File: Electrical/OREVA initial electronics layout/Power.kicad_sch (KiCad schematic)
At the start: 9 parts, among them K1 Contactor_12V_Auto, U2 Buck_Module, U3 Buck_Module, U4 Buck_Module

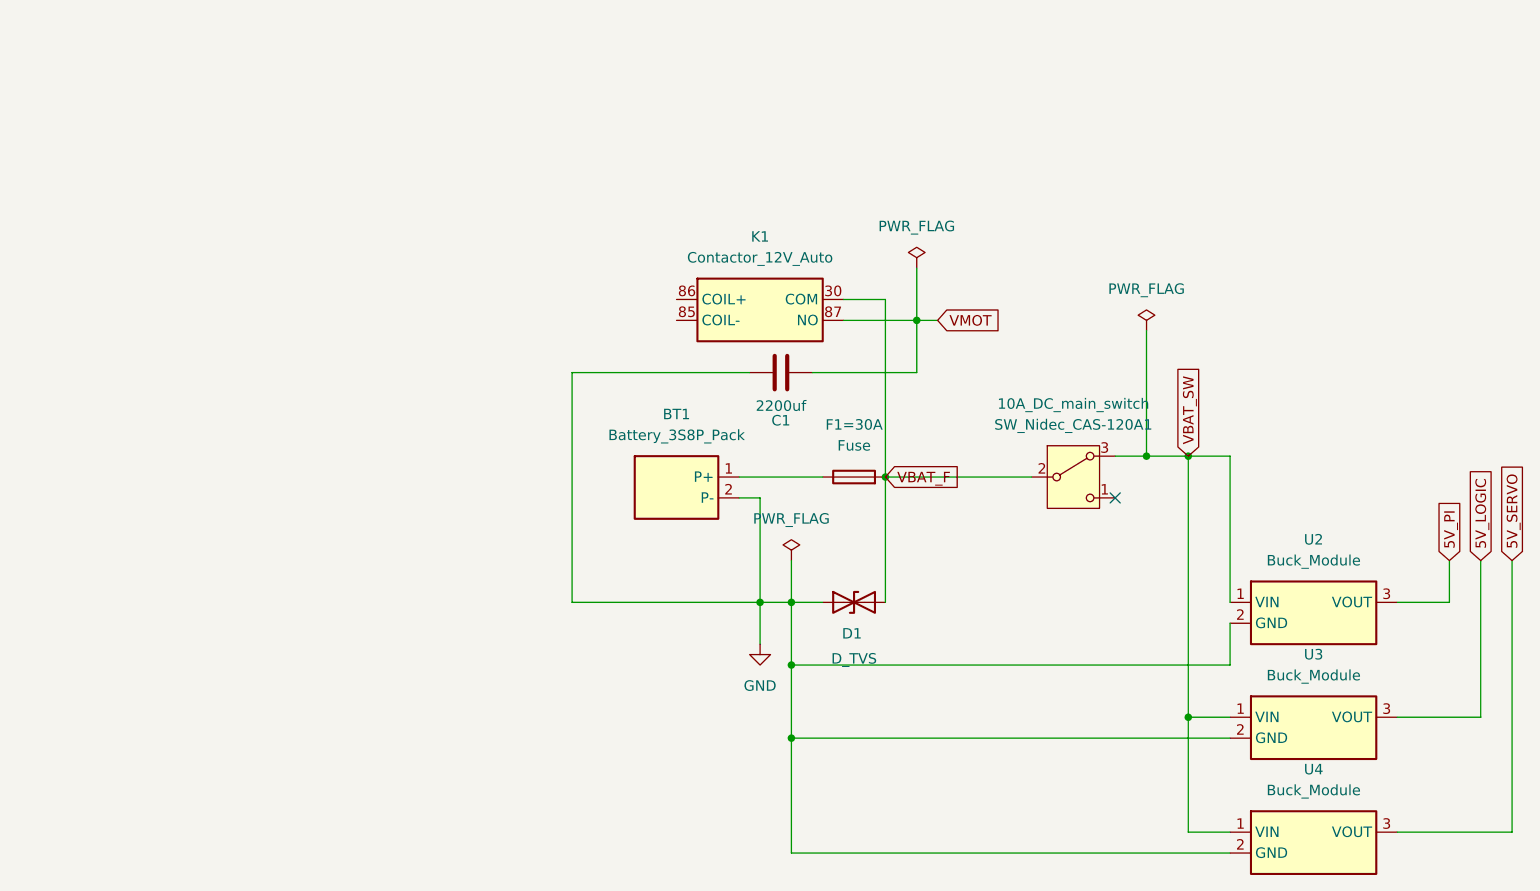
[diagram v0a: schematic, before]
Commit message: Added the MCU block pinout
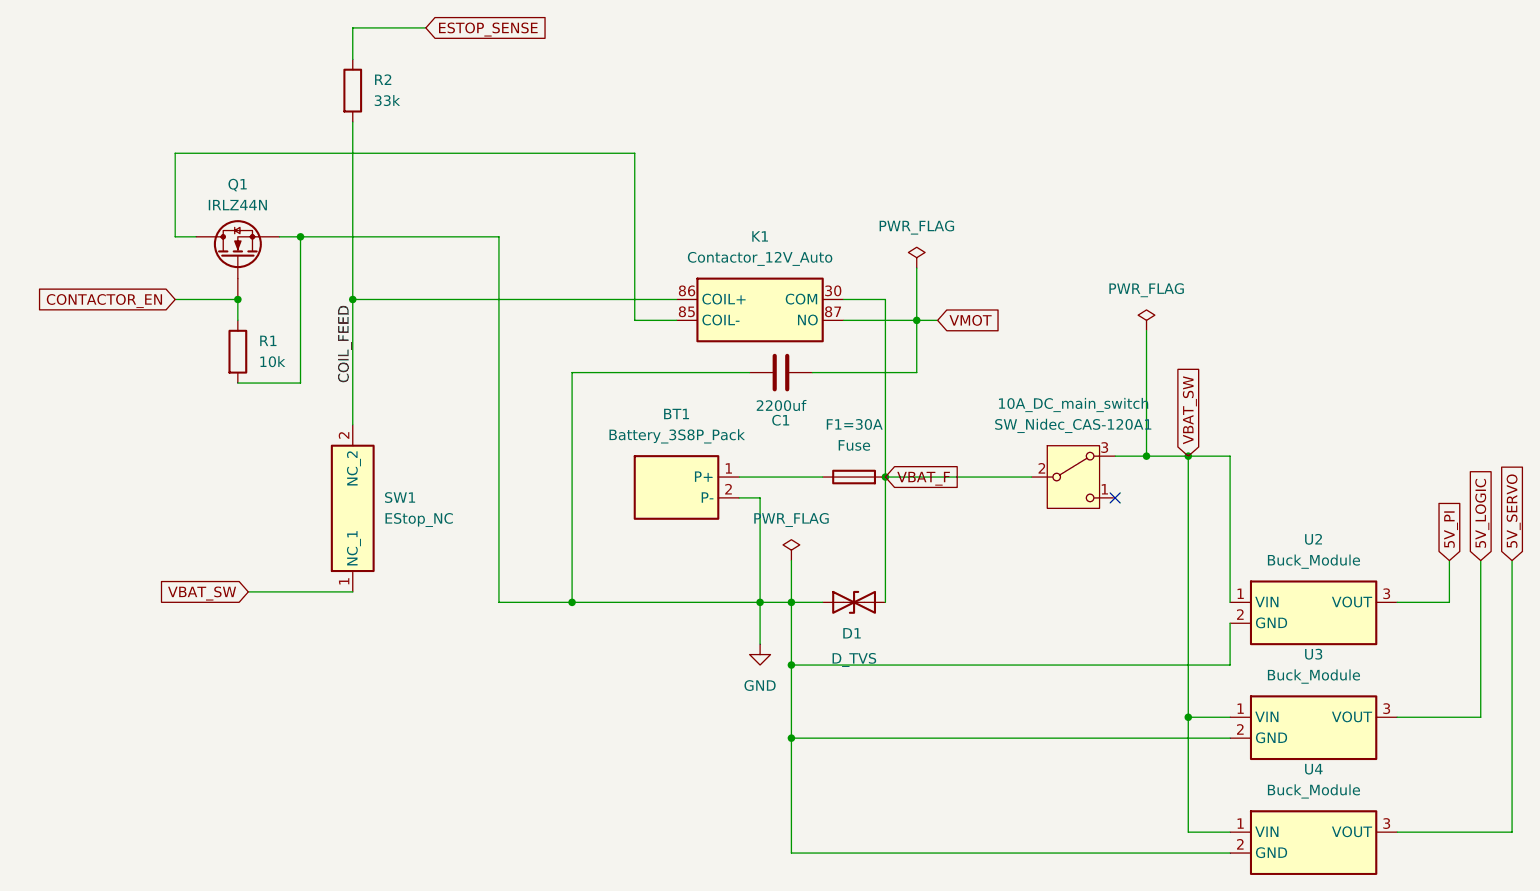
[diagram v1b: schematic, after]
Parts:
- added Q1: IRLZ44N, symbol Device:Q_NMOS
- added R1: 10k, symbol Device:R
- added R2: 33k, symbol Device:R
- added SW1: EStop_NC, symbol OREVA_Custom:EStop_NC
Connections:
- net GND: now also Q1.S, R1.2
- net VBAT_SW: now also SW1.1 (NC_1)
- net at K1.85 (COIL-): now also Q1.D
- net COIL_FEED: now reaches K1.86 (COIL+)
- net COIL_FEED: now also R2.2, SW1.2 (NC_2)
- new net CONTACTOR_EN: Q1.G, R1.1
- new net ESTOP_SENSE: R2.1
